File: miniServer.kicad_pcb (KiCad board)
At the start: 4 copper layers, 30 x 86 mm, 42 parts, among them J1 SI-52008-F, J2 USB_C_Receptacle_USB2.0_16P, J4 MSD-4-A, U1 STM32H725VGTx, U2 LAN8742A, U3 82400102, U4 LT1963AxST-3.3, Y1 ECS-3225MVLC-500-CN-TR

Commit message: Started with pin mapping
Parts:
- added C10: 10pF, Capacitor_SMD:C_0805_2012Metric_Pad1.18x1.45mm_HandSolder, F.Cu at (113.2, 146.0)
- added C11: 10pF, Capacitor_SMD:C_0805_2012Metric_Pad1.18x1.45mm_HandSolder, F.Cu at (118.0, 131.0)
- added C12: 10pF, Capacitor_SMD:C_0805_2012Metric_Pad1.18x1.45mm_HandSolder, F.Cu at (118.0, 134.0)
- added C13: 10pF, Capacitor_SMD:C_0805_2012Metric_Pad1.18x1.45mm_HandSolder, F.Cu at (118.0, 137.0)
- added C14: 22uF, Capacitor_SMD:C_0805_2012Metric_Pad1.18x1.45mm_HandSolder, F.Cu at (118.0, 140.0)
- added C15: 330uF, Capacitor_SMD:C_0805_2012Metric_Pad1.18x1.45mm_HandSolder, F.Cu at (118.0, 143.0)
- added C16: 10uF, Capacitor_SMD:C_0805_2012Metric_Pad1.18x1.45mm_HandSolder, F.Cu at (113.2, 102.6)
- added C17: 10uF, Capacitor_SMD:C_0805_2012Metric_Pad1.18x1.45mm_HandSolder, F.Cu at (113.2, 105.6)
- added C18: 2.2uF, Capacitor_SMD:C_0805_2012Metric_Pad1.18x1.45mm_HandSolder, F.Cu at (113.2, 108.6)
- added C19: 2.2uF, Capacitor_SMD:C_0805_2012Metric_Pad1.18x1.45mm_HandSolder, F.Cu at (113.2, 111.6)
- added C20: 100nF, Capacitor_SMD:C_0805_2012Metric_Pad1.18x1.45mm_HandSolder, F.Cu at (113.2, 114.6)
- added C21: 100nF, Capacitor_SMD:C_0805_2012Metric_Pad1.18x1.45mm_HandSolder, F.Cu at (113.2, 117.7)
- added C22: 100nF, Capacitor_SMD:C_0805_2012Metric_Pad1.18x1.45mm_HandSolder, F.Cu at (118.0, 102.6)
- added C23: 100nF, Capacitor_SMD:C_0805_2012Metric_Pad1.18x1.45mm_HandSolder, F.Cu at (118.0, 105.6)
- added C24: 100nF, Capacitor_SMD:C_0805_2012Metric_Pad1.18x1.45mm_HandSolder, F.Cu at (118.0, 108.6)
- added C25: 100nF, Capacitor_SMD:C_0805_2012Metric_Pad1.18x1.45mm_HandSolder, F.Cu at (118.0, 111.6)
- added C26: 100nF, Capacitor_SMD:C_0805_2012Metric_Pad1.18x1.45mm_HandSolder, F.Cu at (118.0, 114.6)
- added C27: 100nF, Capacitor_SMD:C_0805_2012Metric_Pad1.18x1.45mm_HandSolder, F.Cu at (118.0, 117.7)
- added C28: 100nF, Capacitor_SMD:C_0805_2012Metric_Pad1.18x1.45mm_HandSolder, F.Cu at (122.8, 102.6)
- added C29: 100nF, Capacitor_SMD:C_0805_2012Metric_Pad1.18x1.45mm_HandSolder, F.Cu at (122.8, 105.6)
- added C30: 100nF, Capacitor_SMD:C_0805_2012Metric_Pad1.18x1.45mm_HandSolder, F.Cu at (122.8, 108.6)
- added C31: 100nF, Capacitor_SMD:C_0805_2012Metric_Pad1.18x1.45mm_HandSolder, F.Cu at (122.8, 111.6)
- added C32: 100nF, Capacitor_SMD:C_0805_2012Metric_Pad1.18x1.45mm_HandSolder, F.Cu at (122.8, 114.6)
- added C33: 100nF, Capacitor_SMD:C_0805_2012Metric_Pad1.18x1.45mm_HandSolder, F.Cu at (122.8, 117.7)
- added C34: 100nF, Capacitor_SMD:C_0805_2012Metric_Pad1.18x1.45mm_HandSolder, F.Cu at (127.6, 102.6)
- added C35: 100nF, Capacitor_SMD:C_0805_2012Metric_Pad1.18x1.45mm_HandSolder, F.Cu at (127.6, 105.6)
- added C36: 4.7uF, Capacitor_SMD:C_0805_2012Metric_Pad1.18x1.45mm_HandSolder, F.Cu at (127.6, 108.6)
- added C37: 4.7uF, Capacitor_SMD:C_0805_2012Metric_Pad1.18x1.45mm_HandSolder, F.Cu at (127.6, 111.6)
- added C5: 470pF, Capacitor_SMD:C_0805_2012Metric_Pad1.18x1.45mm_HandSolder, F.Cu at (113.2, 131.0)
- added C6: 1uF, Capacitor_SMD:C_0805_2012Metric_Pad1.18x1.45mm_HandSolder, F.Cu at (113.2, 134.0)
- added C7: 100nF, Capacitor_SMD:C_0805_2012Metric_Pad1.18x1.45mm_HandSolder, F.Cu at (113.2, 137.0)
- added C8: 100nF, Capacitor_SMD:C_0805_2012Metric_Pad1.18x1.45mm_HandSolder, F.Cu at (113.2, 140.0)
- added C9: 100nF, Capacitor_SMD:C_0805_2012Metric_Pad1.18x1.45mm_HandSolder, F.Cu at (113.2, 143.0)
- added J3: Conn_ARM_SWD_TagConnect_TC2030-NL, Connector:Tag-Connect_TC2030-IDC-NL_2x03_P1.27mm_Vertical, F.Cu at (124.6, 121.7)
- added L1: L, Inductor_SMD:L_0805_2012Metric_Pad1.05x1.20mm_HandSolder, F.Cu at (122.8, 142.7)
- added R10: 1.5kR, Resistor_SMD:R_0805_2012Metric_Pad1.20x1.40mm_HandSolder, F.Cu at (122.8, 130.9)
- added R15: 10kR, Resistor_SMD:R_0805_2012Metric_Pad1.20x1.40mm_HandSolder, F.Cu at (122.8, 133.9)
- added R16: 10kR, Resistor_SMD:R_0805_2012Metric_Pad1.20x1.40mm_HandSolder, F.Cu at (122.8, 136.8)
- added R17: 10kR, Resistor_SMD:R_0805_2012Metric_Pad1.20x1.40mm_HandSolder, F.Cu at (122.8, 139.8)
- added R18: 49.9R, Resistor_SMD:R_0805_2012Metric_Pad1.20x1.40mm_HandSolder, F.Cu at (127.5, 130.9)
- added R19: 49.9R, Resistor_SMD:R_0805_2012Metric_Pad1.20x1.40mm_HandSolder, F.Cu at (127.5, 133.9)
- added R20: 49.9R, Resistor_SMD:R_0805_2012Metric_Pad1.20x1.40mm_HandSolder, F.Cu at (127.5, 136.8)
- added R21: 49.9R, Resistor_SMD:R_0805_2012Metric_Pad1.20x1.40mm_HandSolder, F.Cu at (127.5, 139.8)
- added R22: 33R, Resistor_SMD:R_0805_2012Metric_Pad1.20x1.40mm_HandSolder, F.Cu at (132.2, 130.9)
- added R23: 33R, Resistor_SMD:R_0805_2012Metric_Pad1.20x1.40mm_HandSolder, F.Cu at (132.2, 133.9)
- added R24: 33R, Resistor_SMD:R_0805_2012Metric_Pad1.20x1.40mm_HandSolder, F.Cu at (132.2, 136.8)
- added R25: 10kR, Resistor_SMD:R_0805_2012Metric_Pad1.20x1.40mm_HandSolder, F.Cu at (132.2, 139.8)
- added R26: 10kR, Resistor_SMD:R_0805_2012Metric_Pad1.20x1.40mm_HandSolder, F.Cu at (139.0, 130.9)
- added R27: 10kR, Resistor_SMD:R_0805_2012Metric_Pad1.20x1.40mm_HandSolder, F.Cu at (139.0, 133.9)
- added R28: 10kR, Resistor_SMD:R_0805_2012Metric_Pad1.20x1.40mm_HandSolder, F.Cu at (139.0, 136.8)
- added R29: 10kR, Resistor_SMD:R_0805_2012Metric_Pad1.20x1.40mm_HandSolder, F.Cu at (139.0, 139.8)
- added R30: 10kR, Resistor_SMD:R_0805_2012Metric_Pad1.20x1.40mm_HandSolder, F.Cu at (139.0, 142.8)
- added R31: 10kR, Resistor_SMD:R_0805_2012Metric_Pad1.20x1.40mm_HandSolder, F.Cu at (139.0, 145.7)
- added R32: 47R, Resistor_SMD:R_0805_2012Metric_Pad1.20x1.40mm_HandSolder, F.Cu at (132.4, 102.6)
- added R33: 10kR, Resistor_SMD:R_0805_2012Metric_Pad1.20x1.40mm_HandSolder, F.Cu at (132.4, 105.5)
- added R34: 10kR, Resistor_SMD:R_0805_2012Metric_Pad1.20x1.40mm_HandSolder, F.Cu at (132.4, 108.5)
- added U4: LT1963AxST-3.3, Package_TO_SOT_SMD:SOT-223-3_TabPin2, F.Cu at (115.7, 123.4)
- R12: value R -> 10kR
- R6, R9: value 270R -> 10kR
- R7: value 12.1kR 1% -> 12.1kR
- R8: value 4.7kR -> 10kR
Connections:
- net /SDMMC/SDMMC_nDET renamed SDMMC_nDET
- J1 pad 2: unconnected-(J1-COMMON_CT-Pad2) -> /Ethernet/VDDA
- J4 pad 1: /SDMMC/SDMMC_DAT2 -> SDMMC_D2
- J4 pad 2: /SDMMC/SDMMC_DAT3 -> SDMMC_D3
- J4 pad 3: /SDMMC/SDMMC_CMD -> SDMMC_CMD
- J4 pad 5: /SDMMC/SDMMC_CLK -> SDMMC_CK
- J4 pad 7: /SDMMC/SDMMC_DAT0 -> SDMMC_D0
- J4 pad 8: /SDMMC/SDMMC_DAT1 -> SDMMC_D1
- R11 pad 2: /Ethernet/ETH_REF_CLK -> ETH_REF_CLK
- R6 pad 1: /Ethernet/ETH_nRST -> ETH_nINT
- R9 pad 1: /Ethernet/ETH_nINT -> ETH_nRST
- U1 pad 100: unconnected-(U1-VDD-Pad100) -> +3V3
- U1 pad 11: unconnected-(U1-VDDSMPS-Pad11) -> GND
- U1 pad 12: unconnected-(U1-VFBSMPS-Pad12) -> GND
- U1 pad 13: unconnected-(U1-PH0-Pad13) -> RCC_OSC_IN
- U1 pad 14: unconnected-(U1-PH1-Pad14) -> RCC_OSC_OUT
- U1 pad 15: unconnected-(U1-NRST-Pad15) -> nRST
- U1 pad 17: unconnected-(U1-PC1-Pad17) -> ETH_MDC
- U1 pad 20: unconnected-(U1-VDD-Pad20) -> +3V3
- U1 pad 21: Net-(U1-VSS-Pad21) -> GND
- U1 pad 22: unconnected-(U1-VSSA-Pad22) -> GND
- U1 pad 23: unconnected-(U1-VREF+-Pad23) -> Net-(U1-VREF+)
- U1 pad 24: unconnected-(U1-VDDA-Pad24) -> +3V3
- U1 pad 25: unconnected-(U1-PA0-Pad25) -> WKUP1
- U1 pad 26: unconnected-(U1-PA1-Pad26) -> ETH_REF_CLK
- U1 pad 27: unconnected-(U1-PA2-Pad27) -> ETH_MDIO
- U1 pad 29: Net-(U1-VSS-Pad21) -> GND
- U1 pad 30: unconnected-(U1-VDD-Pad30) -> +3V3
- U1 pad 34: unconnected-(U1-PA7-Pad34) -> ETH_CRS_DV
- U1 pad 35: unconnected-(U1-PC4-Pad35) -> ETH_RXD0
- U1 pad 36: unconnected-(U1-PC5-Pad36) -> ETH_RXD1
- U1 pad 4: unconnected-(U1-VDD-Pad4) -> +3V3
- U1 pad 43: unconnected-(U1-PB11-Pad43) -> ETH_TX_EN
- U1 pad 44: unconnected-(U1-VCAP-Pad44) -> Net-(C18-Pad1)
- U1 pad 45: Net-(U1-VSS-Pad21) -> GND
- U1 pad 46: unconnected-(U1-VDDLDO-Pad46) -> +3V3
- U1 pad 47: unconnected-(U1-VDD-Pad47) -> +3V3
- U1 pad 48: unconnected-(U1-PB12-Pad48) -> ETH_TXD0
- U1 pad 49: unconnected-(U1-PB13-Pad49) -> ETH_TXD1
- U1 pad 5: unconnected-(U1-VBAT-Pad5) -> +3V3
- U1 pad 58: Net-(U1-VSS-Pad21) -> GND
- U1 pad 59: unconnected-(U1-VDD-Pad59) -> +3V3
- U1 pad 6: unconnected-(U1-PC13-Pad6) -> ETH_nINT
- U1 pad 62: unconnected-(U1-PC6-Pad62) -> SDMMC_D0
- U1 pad 63: unconnected-(U1-PC7-Pad63) -> SDMMC_D1
- U1 pad 64: unconnected-(U1-PC8-Pad64) -> SDMMC_D0
- U1 pad 65: unconnected-(U1-PC9-Pad65) -> SDMMC_D1
- U1 pad 68: unconnected-(U1-PA10-Pad68) -> /USB/USB_DP
- U1 pad 69: unconnected-(U1-PA11-Pad69) -> /USB/USB_DN
- U1 pad 71: unconnected-(U1-PA13(JTMS-Pad71) -> DEBUG_SWIO
- U1 pad 72: unconnected-(U1-VCAP-Pad72) -> Net-(C18-Pad1)
- U1 pad 73: Net-(U1-VSS-Pad21) -> GND
- U1 pad 74: unconnected-(U1-VDDLDO-Pad74) -> +3V3
- U1 pad 75: unconnected-(U1-VDD-Pad75) -> +3V3
- U1 pad 76: unconnected-(U1-VDD33USB-Pad76) -> +3V3
- U1 pad 77: unconnected-(U1-PA14(JTCK-Pad77) -> DEBUG_SWCLK
- U1 pad 79: unconnected-(U1-PC10-Pad79) -> SDMMC_D2
- U1 pad 80: unconnected-(U1-PC11-Pad80) -> SDMMC_D3
- U1 pad 81: unconnected-(U1-PC12-Pad81) -> SDMMC_CK
- U1 pad 84: unconnected-(U1-PD2-Pad84) -> SDMMC_CMD
- U1 pad 88: unconnected-(U1-VDD-Pad88) -> +3V3
- U1 pad 89: unconnected-(U1-PB3(JTDO-Pad89) -> DEBUG_SWO
- U1 pad 9: unconnected-(U1-VSSSMPS-Pad9) -> GND
- U1 pad 94: unconnected-(U1-BOOT0-Pad94) -> Net-(U1-BOOT0)
- U1 pad 95: unconnected-(U1-PB8-Pad95) -> SDMMC_CK
- U1 pad 97: unconnected-(U1-VCAP-Pad97) -> Net-(C18-Pad1)
- U1 pad 98: Net-(U1-VSS-Pad21) -> GND
- U1 pad 99: unconnected-(U1-VDDLDO-Pad99) -> +3V3
- U2 pad 1: unconnected-(U2-VDD2A-Pad1) -> /Ethernet/VDDA
- U2 pad 11: /Ethernet/ETH_CRS_DV -> ETH_CRS_DV
- U2 pad 12: /Ethernet/ETH_MDIO -> ETH_MDIO
- U2 pad 13: /Ethernet/ETH_MDC -> ETH_MDC
- U2 pad 14: /Ethernet/ETH_nINT -> ETH_nINT
- U2 pad 15: /Ethernet/ETH_nRST -> ETH_nRST
- U2 pad 16: /Ethernet/ETH_TXEN -> ETH_TX_EN
- U2 pad 17: /Ethernet/ETH_TXD0 -> ETH_TXD0
- U2 pad 18: /Ethernet/ETH_TXD1 -> ETH_TXD1
- U2 pad 19: unconnected-(U2-VDD1A-Pad19) -> /Ethernet/VDDA
- U2 pad 5: /Ethernet/ETH_REF_CLK -> ETH_REF_CLK
- U2 pad 6: unconnected-(U2-VDDCR-Pad6) -> Net-(U2-VDDCR)
- U2 pad 7: /Ethernet/ETH_RXD1 -> Net-(U2-RXD1/MODE1)
- U2 pad 8: /Ethernet/ETH_RXD0 -> Net-(U2-RXD0/MODE0)
- U2 pad 9: unconnected-(U2-VDDIO-Pad9) -> +3V3
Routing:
- net ETH_REF_CLK: track 0.00 -> 1.84 mm
- net /Ethernet/ETH_REF_CLK: track 1.84 -> 0.00 mm

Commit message: Added 48MHz quartz
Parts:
- added C38: 830059539, KiCad:830059539, F.Cu at (104.1, 67.8)
- added C39: 22pF, Capacitor_SMD:C_0805_2012Metric_Pad1.18x1.45mm_HandSolder, F.Cu at (102.3, 72.7)
- added C40: 22pF, Capacitor_SMD:C_0805_2012Metric_Pad1.18x1.45mm_HandSolder, F.Cu at (102.3, 75.7)

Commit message: layout v1
no silkscreen done yet
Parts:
- removed C28, C29, C30, C31, C32: 100nF, Capacitor_SMD:C_0805_2012Metric_Pad1.18x1.45mm_HandSolder
- removed the R10 at (68.9, 78.3)
- removed R24: 33R, Resistor_SMD:R_0805_2012Metric_Pad1.20x1.40mm_HandSolder
- removed U4 (x2): LT1963AxST-3.3, Package_TO_SOT_SMD:SOT-223-3_TabPin2
- added J10: Conn_01x01, Connector_Wire:SolderWirePad_1x01_SMD_1.5x3mm, F.Cu at (59.2, 86.9)
- added U5: NCP1117-3.3_SOT223, Package_TO_SOT_SMD:SOT-223-3_TabPin2, B.Cu at (48.5, 120.2)
- C14, C15, C16, C17, D1, D2: moved to B.Cu
- C34, C35: value 100nF -> 4.7uF
- moved R2 136.5 mm to (38.2, 132.6), turned to 90 degrees
- moved R3 134.8 mm to (37.6, 129.5)
- moved R1 132.6 mm to (43.7, 132.6), turned to 90 degrees
- moved C1 128.1 mm to (37.6, 127.5), turned to 180 degrees
- moved D1 119.8 mm to (40.4, 125.3)
- moved D2 119.5 mm to (40.4, 128.8), turned to 180 degrees
- moved C2 113.1 mm to (39.4, 79.6), turned to 90 degrees
- moved R12 110.0 mm to (47.7, 127.5)
- moved R19 103.9 mm to (45.2, 70.4), turned to 180 degrees
- moved R21 102.7 mm to (50.0, 72.4)
- moved R20 101.4 mm to (50.9, 70.4)
- moved R25 101.4 mm to (61.4, 67.3), turned to -90 degrees
- moved R18 100.3 mm to (46.1, 72.4), turned to 180 degrees
- moved R13 97.2 mm to (61.3, 128.7), turned to 180 degrees
- moved R23 97.1 mm to (45.6, 90.1), turned to -90 degrees
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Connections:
- J2 pad A6: /USB/USB_DP -> USB_DP
- J2 pad A7: /USB/USB_DN -> USB_DN
- J2 pad B6: /USB/USB_DP -> USB_DP
- J2 pad B7: /USB/USB_DN -> USB_DN
- U1 pad 50: unconnected-(U1-PB14-Pad50) -> ETH_nRST
- U1 pad 62: SDMMC_D0 -> unconnected-(U1-PC6-Pad62)
- U1 pad 63: SDMMC_D1 -> unconnected-(U1-PC7-Pad63)
- U1 pad 67: unconnected-(U1-PA9-Pad67) -> DEBUG_SWIO
- U1 pad 68: /USB/USB_DP -> unconnected-(U1-PA10-Pad68)
- U1 pad 69: /USB/USB_DN -> USB_DN
- U1 pad 70: unconnected-(U1-PA12-Pad70) -> USB_DP
- U1 pad 78: unconnected-(U1-PA15(JTDI)-Pad78) -> SDMMC_CK
- U1 pad 82: unconnected-(U1-PD0-Pad82) -> SDMMC_nDET
- U1 pad 95: SDMMC_CK -> unconnected-(U1-PB8-Pad95)
- U2 pad 10: Net-(U2-RXER/PHYAD0) -> /Ethernet/ETH_RXER
- U3 pad 1: /USB/USB_DN -> USB_DP
- U3 pad 3: /USB/USB_DP -> USB_DN
- U3 pad 4: /USB/USB_DP -> USB_DN
- U3 pad 6: /USB/USB_DN -> USB_DP
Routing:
- net +3V3: track 0.00 -> 116.0 mm, vias 2 -> 18
- net Net-(D4-A): track 10.8 -> 72.3 mm
- net ETH_nINT: track 0.00 -> 60.1 mm, vias 0 -> 4
- net GND: track 0.00 -> 57.4 mm, vias 0 -> 64
- net /Ethernet/VDDA: track 0.00 -> 52.5 mm, vias 0 -> 2
- net +4V: track 0.00 -> 43.9 mm
- net Net-(J4-COVER_GND): track 0.00 -> 41.6 mm
- net ETH_nRST: track 0.00 -> 41.1 mm, vias 0 -> 2
- net ETH_TXD1: track 0.00 -> 40.0 mm
- net ETH_CRS_DV: track 0.00 -> 40.0 mm
- net ETH_TXD0: track 0.00 -> 40.0 mm
- net ETH_TX_EN: track 0.00 -> 38.1 mm, vias 0 -> 2
- net ETH_REF_CLK: track 1.84 -> 38.9 mm, vias 0 -> 2
- net Net-(U2-LED1/REGOFF): track 0.00 -> 35.9 mm, vias 0 -> 2
- net Net-(C18-Pad1): track 0.00 -> 33.4 mm, vias 0 -> 3
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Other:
- board size 30 x 86 mm -> 30 x 92.9 mm

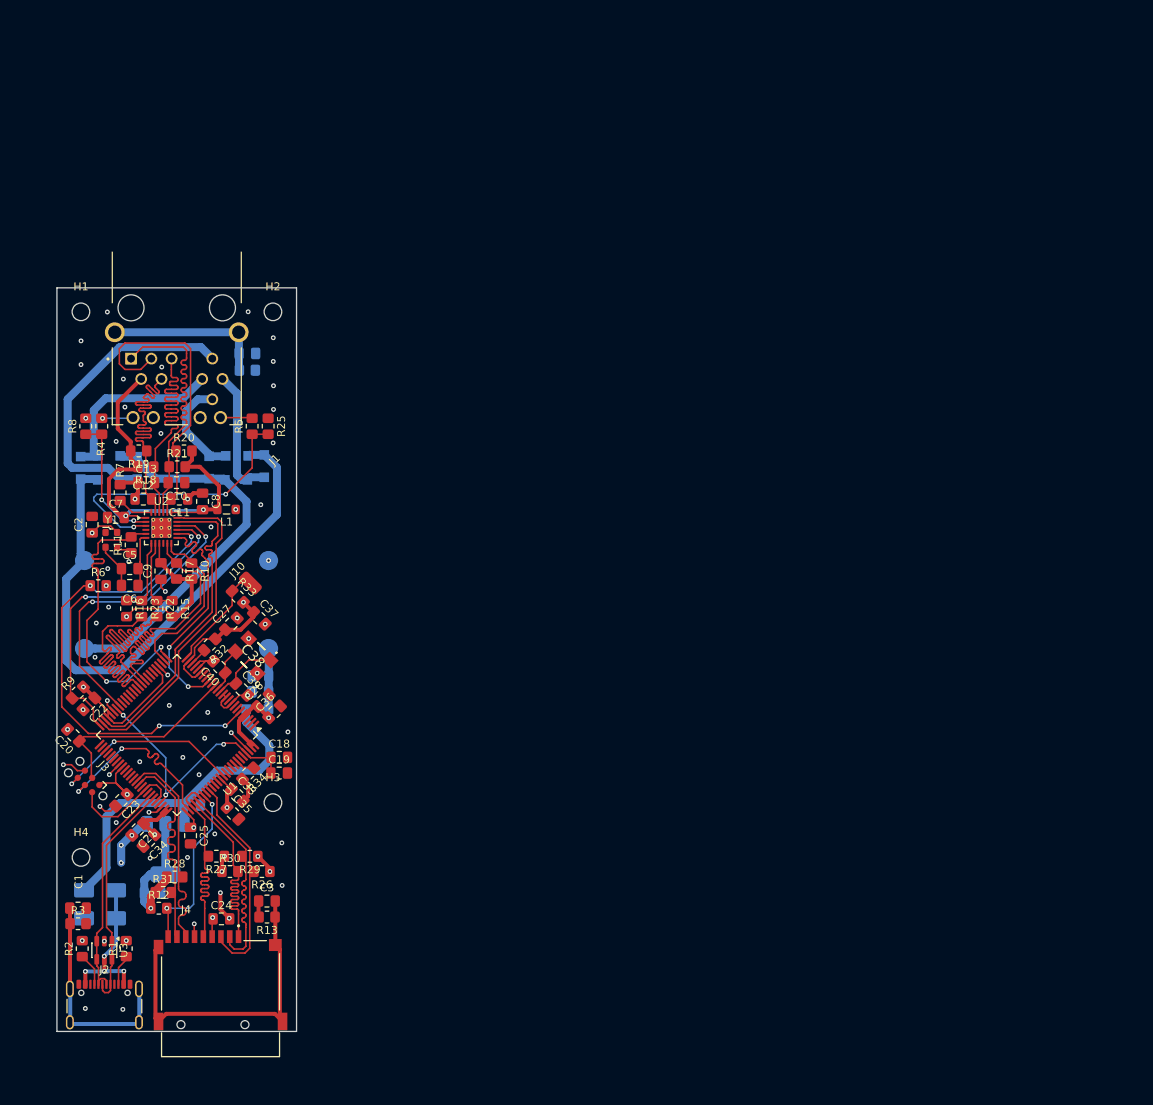
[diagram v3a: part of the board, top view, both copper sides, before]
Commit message: Changed ETH connector, cleared old layout
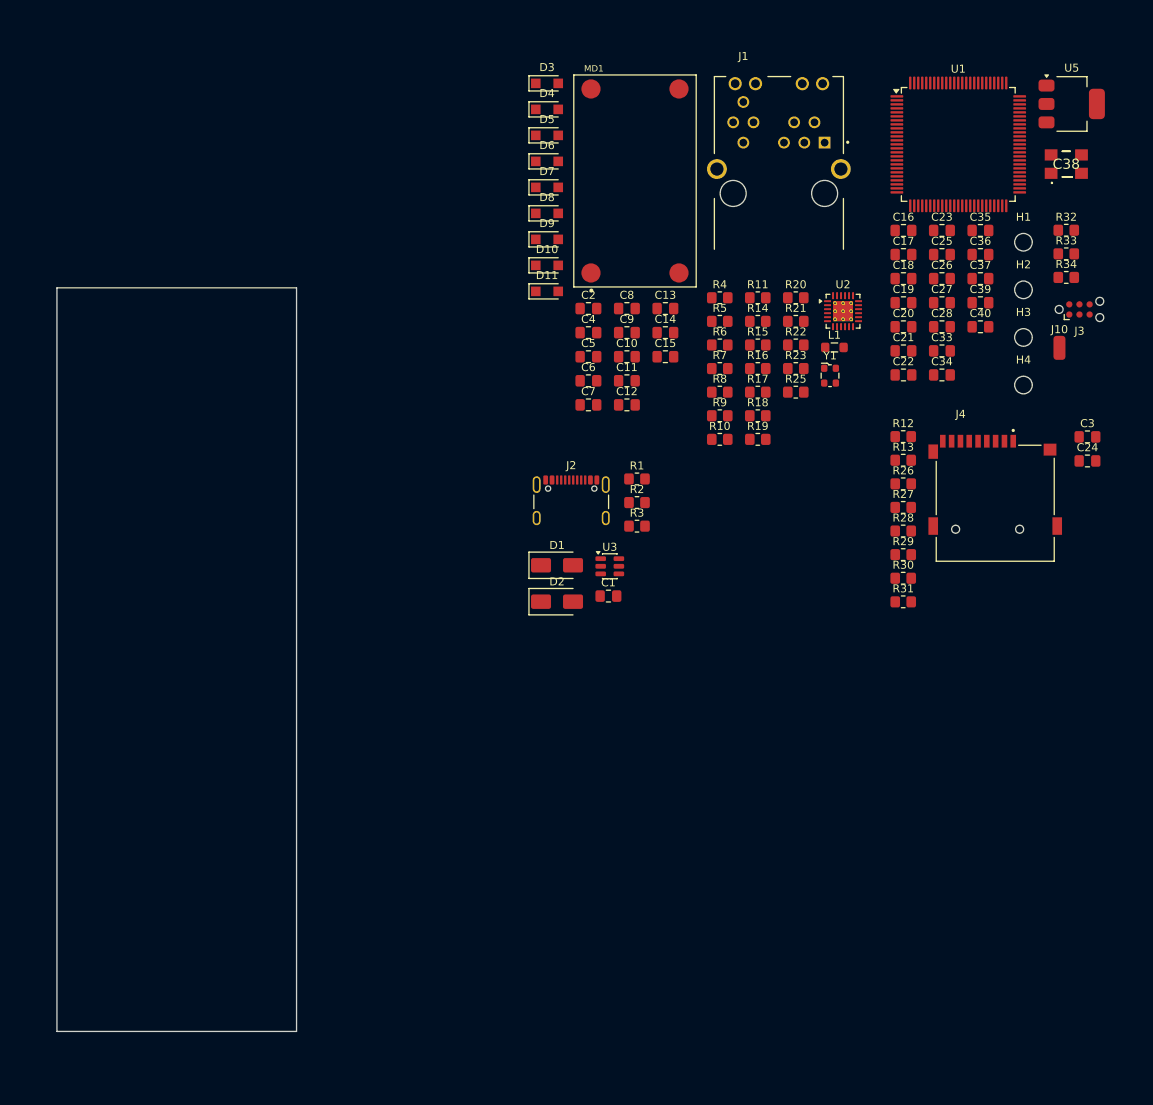
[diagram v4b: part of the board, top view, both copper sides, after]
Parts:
- added C28: 2.2uF, Capacitor_SMD:C_0805_2012Metric_Pad1.18x1.45mm_HandSolder, F.Cu at (145.6, 54.9)
- C14, C15, C16, C17, C4, D1, D10, D11, D2, D3, D4, D5, D6, D7, D8, D9, MD1, R14, U5: moved to F.Cu
- moved U5 146.7 mm to (161.8, 27.0), turned to 0 degrees
- moved J3 137.2 mm to (162.8, 52.7), turned to 0 degrees
- moved H4 131.8 mm to (155.8, 62.1)
- moved C23 124.9 mm to (145.6, 42.8), turned to 0 degrees
- moved C17 123.2 mm to (140.8, 45.8)
- moved C24 122.5 mm to (163.8, 71.6)
- moved U1 122.4 mm to (147.7, 32.1), turned to 0 degrees
- moved R34 119.6 mm to (161.2, 48.7), turned to 0 degrees
- moved R32 118.9 mm to (161.2, 42.8), turned to 0 degrees
- moved C38 118.8 mm to (161.2, 34.5), turned to 0 degrees
- moved C25 118.7 mm to (145.6, 45.8), turned to 0 degrees
- moved C35 118.5 mm to (150.4, 42.8), turned to 0 degrees
- moved H1 118.1 mm to (155.8, 44.3)
- moved C3 117.8 mm to (163.8, 68.6)
- moved C20 115.6 mm to (140.8, 54.9), turned to 0 degrees
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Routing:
- net +3V3: track 116.0 -> 0.00 mm, vias 18 -> 0
- net Net-(D4-A): track 72.3 -> 0.00 mm
- net ETH_nINT: track 60.1 -> 0.00 mm, vias 4 -> 0
- net GND: track 57.4 -> 0.00 mm, vias 64 -> 0
- net /Ethernet/VDDA: track 52.5 -> 0.00 mm, vias 2 -> 0
- net Net-(D10-K): track 48.0 -> 0.00 mm
- net +4V: track 43.9 -> 0.00 mm
- net Net-(J4-COVER_GND): track 41.6 -> 0.00 mm
- net ETH_nRST: track 41.1 -> 0.00 mm, vias 2 -> 0
- net ETH_TXD1: track 40.0 -> 0.00 mm
- net ETH_CRS_DV: track 40.0 -> 0.00 mm
- net ETH_TXD0: track 40.0 -> 0.00 mm
- net ETH_REF_CLK: track 38.9 -> 0.00 mm, vias 2 -> 0
- net Net-(D3-A): track 38.9 -> 0.00 mm
- net ETH_TX_EN: track 38.1 -> 0.00 mm, vias 2 -> 0
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
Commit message: Started layout v2
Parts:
- removed C16, C17: 10uF, Capacitor_SMD:C_0805_2012Metric_Pad1.18x1.45mm_HandSolder
- added C29: 10uF, Capacitor_SMD:C_0805_2012Metric_Pad1.18x1.45mm_HandSolder, F.Cu at (-17.3, 37.5)
- added C30: 10uF, Capacitor_SMD:C_0805_2012Metric_Pad1.18x1.45mm_HandSolder, F.Cu at (-17.3, 40.5)
- added D12: LED, LED_SMD:LED_0805_2012Metric_Pad1.15x1.40mm_HandSolder, F.Cu at (-26.8, 27.8)
- added D13: LED, LED_SMD:LED_0805_2012Metric_Pad1.15x1.40mm_HandSolder, F.Cu at (-26.8, 30.8)
- added J5: 0826-1X1T-GJ-F, 0826_1X1T_GJ_F:BEL_0826-1X1T-GJ-F, F.Cu at (49.4, 55.8)
- added J6: Conn_01x03_Pin, Connector_Wire:SolderWire-0.15sqmm_1x03_P4mm_D0.5mm_OD1.5mm, F.Cu at (-22.4, 22.1)
- added R24: 280R, Resistor_SMD:R_0805_2012Metric_Pad1.20x1.40mm_HandSolder, F.Cu at (-22.0, 25.4)
- added R35: 280R, Resistor_SMD:R_0805_2012Metric_Pad1.20x1.40mm_HandSolder, F.Cu at (-22.0, 28.4)
- added R36: 280R, Resistor_SMD:R_0805_2012Metric_Pad1.20x1.40mm_HandSolder, F.Cu at (-22.0, 31.3)
- added R37: 110R, Resistor_SMD:R_0805_2012Metric_Pad1.20x1.40mm_HandSolder, F.Cu at (-22.0, 34.3)
- D1: value D_Schottky -> WE-TVS_SOT23-6L_82402305; footprint Diode_SMD:D_SMA -> 82402305:WE-TVS_SOT23-6L
- D11: value D_Schottky -> LED; footprint Diode_SMD:Nexperia_CFP3_SOD-123W -> LED_SMD:LED_0805_2012Metric_Pad1.15x1.40mm_HandSolder
- D2: value SMAJ6.0A 6V -> LED; footprint Diode_SMD:D_SMA -> LED_SMD:LED_0805_2012Metric_Pad1.15x1.40mm_HandSolder
- D4, D6, D7, D8: moved to B.Cu
- J1: value SI-52008-F -> Conn_01x02_Pin; footprint SI_52008_F:BEL_SI-52008-F -> Connector_Wire:SolderWire-0.15sqmm_1x02_P4mm_D0.5mm_OD1.5mm
- L1: value L -> 2A/50mOhm
- moved U5 176.6 mm to (-14.7, 28.1)
- moved C14 148.6 mm to (-33.6, 21.7)
- moved C15 148.6 mm to (-33.6, 24.7)
- moved J1 142.9 mm to (-17.6, 34.1)
- moved D2 141.4 mm to (-26.8, 21.7)
- moved D11 125.7 mm to (-26.8, 24.8)
- moved U2 94.2 mm to (49.6, 96.1)
- moved R20 84.4 mm to (51.4, 88.1), turned to 180 degrees
- moved R21 83.1 mm to (52.4, 90.0), turned to 180 degrees
- moved R7 79.9 mm to (44.7, 92.2)
- moved MD1 79.5 mm to (34.4, 70.7), turned to 180 degrees
- moved R19 78.8 mm to (46.7, 90.0)
- moved R4 78.4 mm to (44.5, 78.8)
- moved R18 78.1 mm to (47.7, 88.1)
- moved R8 77.4 mm to (42.5, 80.7), turned to 180 degrees
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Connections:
- C10 pad 2: Net-(J1-TD+) -> Net-(J5-TRD1+)
- C11 pad 2: Net-(J1-TD-) -> Net-(J5-TRD1-)
- C12 pad 2: Net-(J1-RD+) -> Net-(J5-TRD2+)
- C13 pad 2: Net-(J1-RD-) -> Net-(J5-TRD2-)
- C14 pad 2: Net-(D11-A) -> +PoE
- C15 pad 2: Net-(D11-A) -> +PoE
- C4 pad 2: Net-(J1-SHIELD) -> Net-(J5-SHIELD)
- D1 pad 1: +4V -> Net-(J5-TRD1-)
- D1 pad 2: /USB/VBUS -> GND
- D10 pad 2: Net-(D10-A) -> /Ethernet/PoE/V2-
- D11 pad 1: +4V -> Net-(D11-K)
- D11 pad 2: Net-(D11-A) -> +VBUS
- D2 pad 1: /USB/VBUS -> Net-(D2-K)
- D2 pad 2: GND -> +Vin_5V
- D3 pad 2: Net-(D3-A) -> /Ethernet/PoE/V1-
- D4 pad 1: Net-(D4-K) -> /Ethernet/PoE/V1+
- D5 pad 1: Net-(D3-A) -> /Ethernet/PoE/V1-
- D6 pad 1: Net-(D6-K) -> /Ethernet/PoE/V2+
- D7 pad 2: Net-(D4-K) -> /Ethernet/PoE/V1+
- D8 pad 2: Net-(D6-K) -> /Ethernet/PoE/V2+
- D9 pad 1: Net-(D10-A) -> /Ethernet/PoE/V2-
- J1 pad 1: Net-(J1-TD+) -> GND
- J1 pad 2: /Ethernet/VDDA -> GND
- J2 pad A4: /USB/VBUS -> +VBUS
- J2 pad A9: /USB/VBUS -> +VBUS
- J2 pad B4: /USB/VBUS -> +VBUS
- J2 pad B9: /USB/VBUS -> +VBUS
- MD1 pad 4: Net-(D11-A) -> +PoE
- R14 pad 1: Net-(J1-SHIELD) -> Net-(J5-SHIELD)
- R18 pad 1: Net-(J1-RD-) -> Net-(J5-TRD2-)
- R19 pad 1: Net-(J1-RD+) -> Net-(J5-TRD2+)
- R20 pad 1: Net-(J1-TD-) -> Net-(J5-TRD1-)
- R21 pad 1: Net-(J1-TD+) -> Net-(J5-TRD1+)
- R4 pad 2: Net-(J1-PadY_K) -> Net-(J5-Pad18)
- R5 pad 2: Net-(J1-PadG_A) -> Net-(J5-Pad19)
- U2 pad 20: Net-(J1-TD-) -> Net-(J5-TRD1+)
- U2 pad 21: Net-(J1-TD+) -> Net-(J5-TRD1-)
- U2 pad 22: Net-(J1-RD-) -> Net-(J5-TRD2-)
- U2 pad 23: Net-(J1-RD+) -> Net-(J5-TRD2+)
- U3 pad 5: /USB/VBUS -> +VBUS
- U5 pad 3: +4V -> +Vin_5V
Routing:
- net /Ethernet/VDDA: track 0.00 -> 41.9 mm, vias 0 -> 3
- net /Ethernet/PoE/V1-: track 0.00 -> 30.7 mm
- net /Ethernet/PoE/V2-: track 0.00 -> 28.4 mm
- net Net-(J5-TRD2-): track 0.00 -> 28.0 mm
- net Net-(J5-TRD2+): track 0.00 -> 27.9 mm
- net Net-(J5-TRD1+): track 0.00 -> 27.9 mm
- net Net-(J5-TRD1-): track 0.00 -> 27.9 mm
- net Net-(D4-A): track 0.00 -> 26.0 mm, vias 0 -> 1
- net Net-(D10-K): track 0.00 -> 25.1 mm, vias 0 -> 1
- net /Ethernet/PoE/V1+: track 0.00 -> 22.4 mm
- net Net-(U2-LED2/~{INTSEL}): track 0.00 -> 22.2 mm
- net /Ethernet/PoE/V2+: track 0.00 -> 19.5 mm
- net GND: track 0.00 -> 6.91 mm, vias 0 -> 5
- net +3V3: track 0.00 -> 5.58 mm
- net Net-(U2-RBIAS): track 0.00 -> 3.76 mm
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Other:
- board outline removed
